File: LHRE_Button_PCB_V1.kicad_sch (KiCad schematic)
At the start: 19 parts, among them J1 Conn_01x12_Female, J2 Conn_01x12_Female, J3 Conn_01x02_Female, SW1 Dashboard_Button, SW2 Dashboard_Button, SW3 Dashboard_Button, SW4 Dashboard_Button, SW5 Dashboard_Button, SW6 Dashboard_Button

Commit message: board proto
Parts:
- added J3: Conn_01x02_Female, Connector_Wire:SolderWire-0.1sqmm_1x02_P3.6mm_D0.4mm_OD1mm, symbol Connector:Conn_01x02_Female
- J1, J2: footprint (none) -> Connector_Molex:Molex_Micro-Fit_3.0_43650-1210_1x12-1MP_P3.00mm_Horizontal
- J4: renamed from J3; footprint (none) -> Connector_Molex:Molex_Micro-Fit_3.0_43650-0210_1x02-1MP_P3.00mm_Horizontal
- R1: footprint Resistor_SMD:R_0201_0603Metric -> Resistor_SMD:R_0603_1608Metric
- R2: renamed from R3; footprint Resistor_SMD:R_0201_0603Metric -> Resistor_SMD:R_0603_1608Metric
- R3: renamed from R4; footprint Resistor_SMD:R_0201_0603Metric -> Resistor_SMD:R_0603_1608Metric
- R4: renamed from R5; footprint Resistor_SMD:R_0201_0603Metric -> Resistor_SMD:R_0603_1608Metric
- R5: renamed from R6; footprint Resistor_SMD:R_0201_0603Metric -> Resistor_SMD:R_0603_1608Metric
- R6: renamed from R7; footprint Resistor_SMD:R_0201_0603Metric -> Resistor_SMD:R_0603_1608Metric
- R7: renamed from R8; footprint Resistor_SMD:R_0201_0603Metric -> Resistor_SMD:R_0603_1608Metric
- R8: renamed from R2; footprint Resistor_SMD:R_0201_0603Metric -> Resistor_SMD:R_0603_1608Metric
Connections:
- net 12V_L: now also J1.11 (Pin_11), J1.5 (Pin_5), SW1.1, SW2.1, SW3.1; no longer J1.10 (Pin_10), J1.12 (Pin_12), SW1. (5), SW2. (5), SW3. (5)
- net 12V_R: now also J2.11 (Pin_11), J2.5 (Pin_5), SW4.1, SW5.1, SW6.1; no longer J2.10 (Pin_10), J2.12 (Pin_12), SW4. (5), SW5. (5), SW6. (5)
- net AMS: now also J1.12 (Pin_12); no longer J1.3 (Pin_3)
- net GND: now also SW4.5, SW5.5, SW6.5; no longer D1.1 (K), J1.1 (Pin_1), R2.1, R3.1, R4.1, SW1. (5), SW2. (5), SW3. (5), SW4. (5), SW5. (5), SW6. (5)
- net IMD: now also J2.12 (Pin_12); no longer J2.3 (Pin_3)
- net MCU_SIG1: now also J1.10 (Pin_10), SW1.4; no longer J1.6 (Pin_6), SW1. (5)
- net MCU_SIG2: now also J1.7 (Pin_7), SW2.4; no longer J1.5 (Pin_5), SW2. (5)
- net MCU_SIG3: now also SW3.4; no longer SW3. (5)
- net MCU_SIG4: now also J2.10 (Pin_10), SW4.4; no longer J2.6 (Pin_6), SW4. (5)
- net MCU_SIG5: now also J2.7 (Pin_7), SW5.4; no longer J2.5 (Pin_5), SW5. (5)
- net MCU_SIG6: now also SW6.4; no longer SW6. (5)
- net SHTDWN_IN: now also J3.1 (Pin_1)
- net SHTDWN_OUT: now also J3.2 (Pin_2)
- net SW1_OUT: now also J1.9 (Pin_9), SW1.2; no longer J1.11 (Pin_11), SW1. (5)
- net SW2_OUT: now also J1.6 (Pin_6), SW2.2; no longer J1.9 (Pin_9), SW2. (5)
- net SW3_OUT: now also J1.3 (Pin_3), SW3.2; no longer J1.7 (Pin_7), SW3. (5)
- net SW4_OUT: now also J2.9 (Pin_9), SW4.2; no longer J2.11 (Pin_11), SW4. (5)
- net SW5_OUT: now also J2.6 (Pin_6), SW5.2; no longer J2.9 (Pin_9), SW5. (5)
- net SW6_OUT: now also J2.3 (Pin_3), SW6.2; no longer J2.7 (Pin_7), SW6. (5)
- new net GND1: D1.1 (K), J1.1 (Pin_1), R2.1, R3.1, R4.1, SW1.5, SW2.5, SW3.5
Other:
- removed sheet SEPIC_CAD_L
- added sheet SEPIC_CAD (SEPIC_L.kicad_sch)
- sheet SEPIC_CAD_R: file ../AccumulatorHUD_2023/2023KicadLibrary-main/Standardized Subsheets/SEPIC_CAD.kicad_sch -> ../../AccumulatorHUD_2023/2023KicadLibrary-main/Standardized Subsheets/SEPIC_CAD.kicad_sch

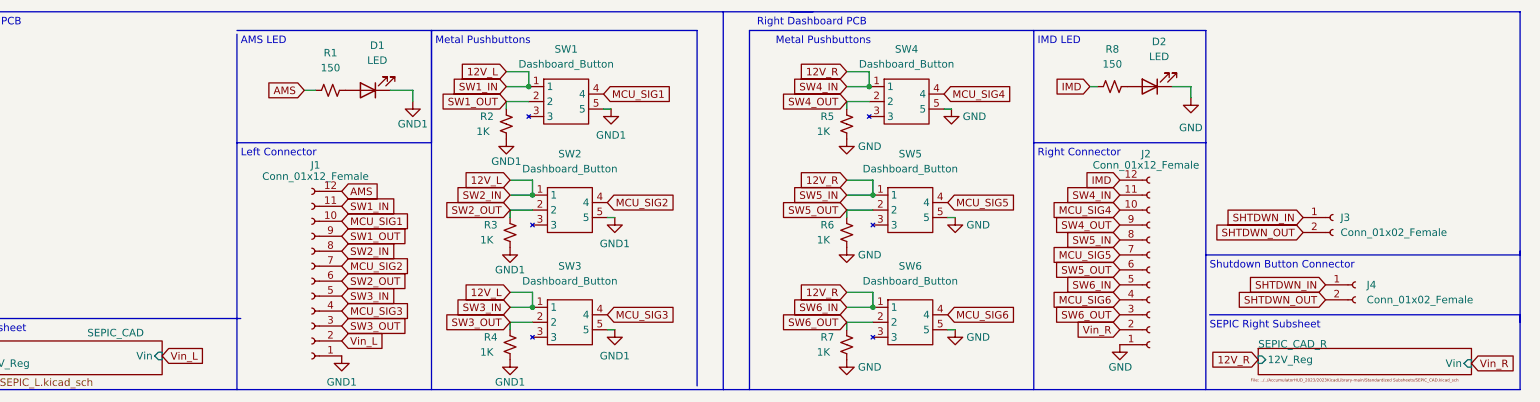
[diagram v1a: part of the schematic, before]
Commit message: updated dash PCB
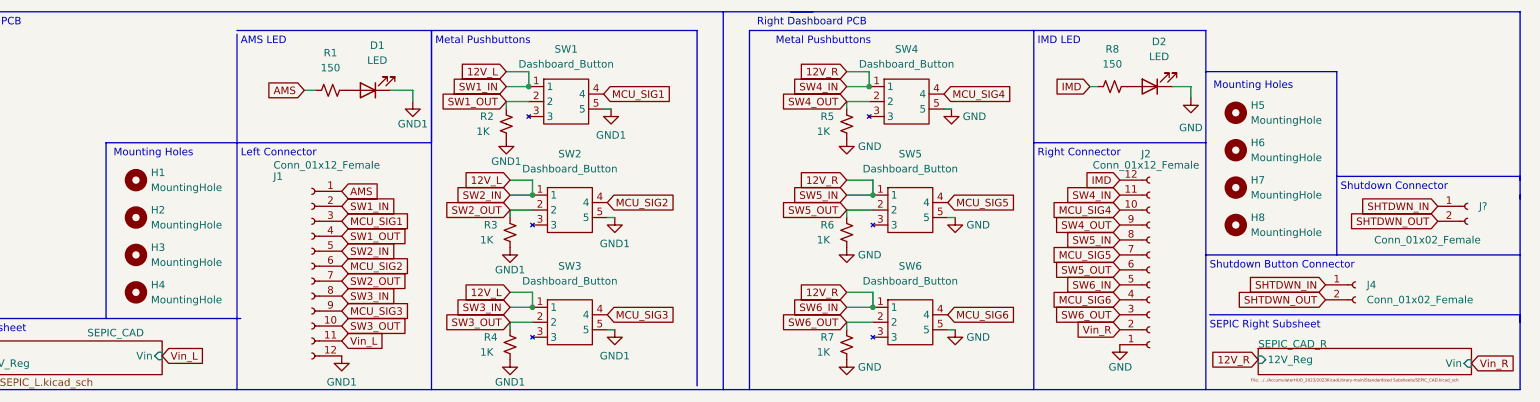
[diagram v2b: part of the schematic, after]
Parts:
- removed J3: Conn_01x02_Female, Connector_Wire:SolderWire-0.1sqmm_1x02_P3.6mm_D0.4mm_OD1mm, symbol Connector:Conn_01x02_Female
- added H1, H2, H3, H4, H5, H6, H7, H8: MountingHole, MountingHole:MountingHole_3.5mm, symbol Mechanical:MountingHole
- added J?: Conn_01x02_Female, Connector_Wire:SolderWire-0.5sqmm_1x02_P4.8mm_D0.9mm_OD2.3mm, symbol Connector:Conn_01x02_Female
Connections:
- net 12V_L: now also J1.2 (Pin_2); no longer J1.11 (Pin_11)
- net AMS: now also J1.1 (Pin_1); no longer J1.12 (Pin_12)
- net GND1: now also J1.12 (Pin_12); no longer J1.1 (Pin_1)
- net MCU_SIG1: now also J1.3 (Pin_3); no longer J1.10 (Pin_10)
- net MCU_SIG2: now also J1.6 (Pin_6); no longer J1.7 (Pin_7)
- net MCU_SIG3: now also J1.9 (Pin_9); no longer J1.4 (Pin_4)
- net SHTDWN_IN: now also J?.1 (Pin_1)
- net SHTDWN_OUT: now also J?.2 (Pin_2)
- net SW1_OUT: now also J1.4 (Pin_4); no longer J1.9 (Pin_9)
- net SW2_OUT: now also J1.7 (Pin_7); no longer J1.6 (Pin_6)
- net SW3_OUT: now also J1.10 (Pin_10); no longer J1.3 (Pin_3)
- net Vin_L: now also J1.11 (Pin_11); no longer J1.2 (Pin_2)
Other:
- note added: "Mounting Holes"
- note added: "Shutdown Connector"
- moved on the sheet: J1

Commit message: REV2
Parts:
- removed D1, D2: LED, Dashboard_LED:LEDC1608X80N, symbol Device:LED
- removed J1, J2: Conn_01x12_Female, Connector_Molex:Molex_Micro-Fit_3.0_43650-1210_1x12-1MP_P3.00mm_Horizontal, symbol Connector:Conn_01x12_Female
- removed J4: Conn_01x02_Female, Connector_Molex:Molex_Micro-Fit_3.0_43650-0210_1x02-1MP_P3.00mm_Horizontal, symbol Connector:Conn_01x02_Female
- removed J?: Conn_01x02_Female, Connector_Wire:SolderWire-0.5sqmm_1x02_P4.8mm_D0.9mm_OD2.3mm, symbol Connector:Conn_01x02_Female
- removed R7: 1K, Resistor_SMD:R_0603_1608Metric, symbol Device:R_Small_US
- removed SW2, SW3, SW4: Dashboard_Button, Dashboard_LED:Dashboard_Btn, symbol Dashboard:Dashboard_Button
- added J1, J2, J3, J7: Conn_01x02, Connector_Molex:Molex_Micro-Fit_3.0_43650-0215_1x02_P3.00mm_Vertical, symbol Connector_Generic:Conn_01x02
- added J4, J5: Conn_01x08, Connector_Molex:Molex_Micro-Fit_3.0_43650-0800_1x08_P3.00mm_Horizontal, symbol Connector_Generic:Conn_01x08
- added J6: Conn_01x12, Connector_Molex:Molex_Micro-Fit_3.0_43045-1212_2x06_P3.00mm_Vertical, symbol Connector_Generic:Conn_01x12
- added R1, R12, R13, R14, R15, R16, R17: 10k, Resistor_SMD:R_0603_1608Metric, symbol Device:R_Small_US
- added R10, R11, R18, R19, R20, R9: 470, Resistor_SMD:R_0603_1608Metric, symbol Device:R_Small_US
- added SW1, SW2, SW3, SW7, SW8, SW9: SW_DIP_x06, Through_DIP_6:18253604, symbol Switch:SW_DIP_x06
- added SW10, SW11, SW12: Dashboard_Button, Dashboard_LED:Dashboard_Btn, symbol Dashboard:Dashboard_Button
- R2, R3, R4, R5, R6: value 1K -> 10k
- renumbered R1 to R7, SW1 to SW4
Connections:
- net 12V_L: now also R3.1, R5.1, R1.1, SW1.5, SW2.5, SW3.5; no longer SW4.1
- net 12V_R: now also R12.1, R14.1, R16.1, SW7.5, SW8.5, SW9.5; no longer SW5.1, SW6.1
- net AMS: now also J4.2 (Pin_2)
- net GND: now also J2.2 (Pin_2), J5.1 (Pin_1), J6.6 (Pin_6), R13.1, R15.1, R17.1, SW7.6, SW8.6, SW9.6; no longer R5.1, R6.1, SW5.5, SW6.5
- net GND1: now also R6.1, J1.2 (Pin_2), J4.8 (Pin_8), SW1.6, SW2.6, SW3.6; no longer R3.1, SW4.5
- net IMD: now also J6.7 (Pin_7)
- net SHTDWN_IN: now also J3.1 (Pin_1), J6.10 (Pin_10)
- net SHTDWN_OUT: now also J4.4 (Pin_4), J7.2 (Pin_2)
- net SW1_OUT: now also J4.1 (Pin_1), SW1.3, SW1.4; no longer R2.2
- net SW2_OUT: now also SW5.2, J4.3 (Pin_3), SW2.3, SW2.4; no longer R3.2
- net SW3_OUT: now also SW6.2, J4.6 (Pin_6), SW3.3, SW3.4; no longer R4.2
- net SW4_OUT: now also J6.4 (Pin_4), SW10.2, SW7.3, SW7.4; no longer R5.2
- net SW5_OUT: now also J6.5 (Pin_5), SW11.2, SW8.3, SW8.4; no longer R6.2, SW5.2
- net SW6_OUT: now also J6.12 (Pin_12), SW12.2, SW9.3, SW9.4; no longer SW6.2
- net Vin_L: now also J4.7 (Pin_7)
- net Vin_R: now also J5.2 (Pin_2), J6.11 (Pin_11)
- net at R8.2: now also J2.1 (Pin_1)
- net at R7.2: now also J1.1 (Pin_1)
- net MCU_SIG1 renamed P11
- net P11: now also SW1.10, SW1.8
- net MCU_SIG5 renamed P21
- net P21: now also SW2.10, SW2.8
- net MCU_SIG6 renamed P31
- net P31: now also SW3.10, SW3.8
- new net: R11.2, SW6.5
- new net: R19.2, SW11.5
- new net: R5.2, SW3.2
- new net: R15.2, SW8.1
- new net: R18.2, SW10.5
- new net: R10.2, SW5.5
- new net: R17.2, SW9.1
- new net: R4.2, SW2.1
- new net: R3.2, SW2.2
- new net: R16.2, SW9.2
- new net: R9.2, SW4.5
- new net: R6.2, SW3.1
- new net: R20.2, SW12.5
- new net: R14.2, SW8.2
- new net: R13.2, SW7.1
- new net: R1.2, SW1.2
- new net: R12.2, SW7.2
- new net: R2.2, SW1.1
- new net AMS_R: J5.7 (Pin_7), J6.8 (Pin_8)
- new net G11: R9.1, SW1.7, SW1.9
- new net G21: R10.1, SW2.7, SW2.9
- new net G31: R11.1, SW3.7, SW3.9
- new net G41: R18.1, SW7.7, SW7.9
- new net G51: R19.1, SW8.7, SW8.9
- new net G61: R20.1, SW9.7, SW9.9
- new net INRTA_IN: J4.5 (Pin_5), J7.1 (Pin_1)
- new net INRTA_IN_R: J3.2 (Pin_2), J5.4 (Pin_4)
- new net P41: SW10.4, SW7.10, SW7.8
- new net P51: SW11.4, SW8.10, SW8.8
- new net P61: SW12.4, SW9.10, SW9.8
- new net SHTDWN_OUT_R: J5.5 (Pin_5), J6.9 (Pin_9)
- new net SW1_IN: SW1.11, SW1.12, SW4.1
- new net SW1_OUT_R: J5.8 (Pin_8), J6.1 (Pin_1)
- new net SW2_IN: SW2.11, SW2.12, SW5.1
- new net SW2_OUT_R: J5.6 (Pin_6), J6.2 (Pin_2)
- new net SW3_IN: SW3.11, SW3.12, SW6.1
- new net SW3_OUT_R: J5.3 (Pin_3), J6.3 (Pin_3)
- new net SW4_IN: SW10.1, SW7.11, SW7.12
- new net SW5_IN: SW11.1, SW8.11, SW8.12
- new net SW6_IN: SW12.1, SW9.11, SW9.12
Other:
- removed sheet SEPIC_CAD_R
- note added: "Exit Connector Left"
- note added: "Exit Connector Right"
- note added: "In Connector Right"
- note added: "Inertia Switch"
- note added: "Latching Buttons"
- note added: "Momentary Buttons"
- note added: "Mounting Holes Left"
- note added: "Mounting Holes Right"
- note removed: "Left Connector"
- note removed: "Left Dashboard PCB"
- note removed: "Metal Pushbuttons"
- note removed: "Mounting Holes"
- note removed: "Right Connector"
- note removed: "Right Dashboard PCB"
- note removed: "SEPIC Right Subsheet"
- note removed: "Shutdown Button Connector"
- moved on the sheet: H1, H2, H3, H4, H5, H6, H7, H8, R7, R8, SW4

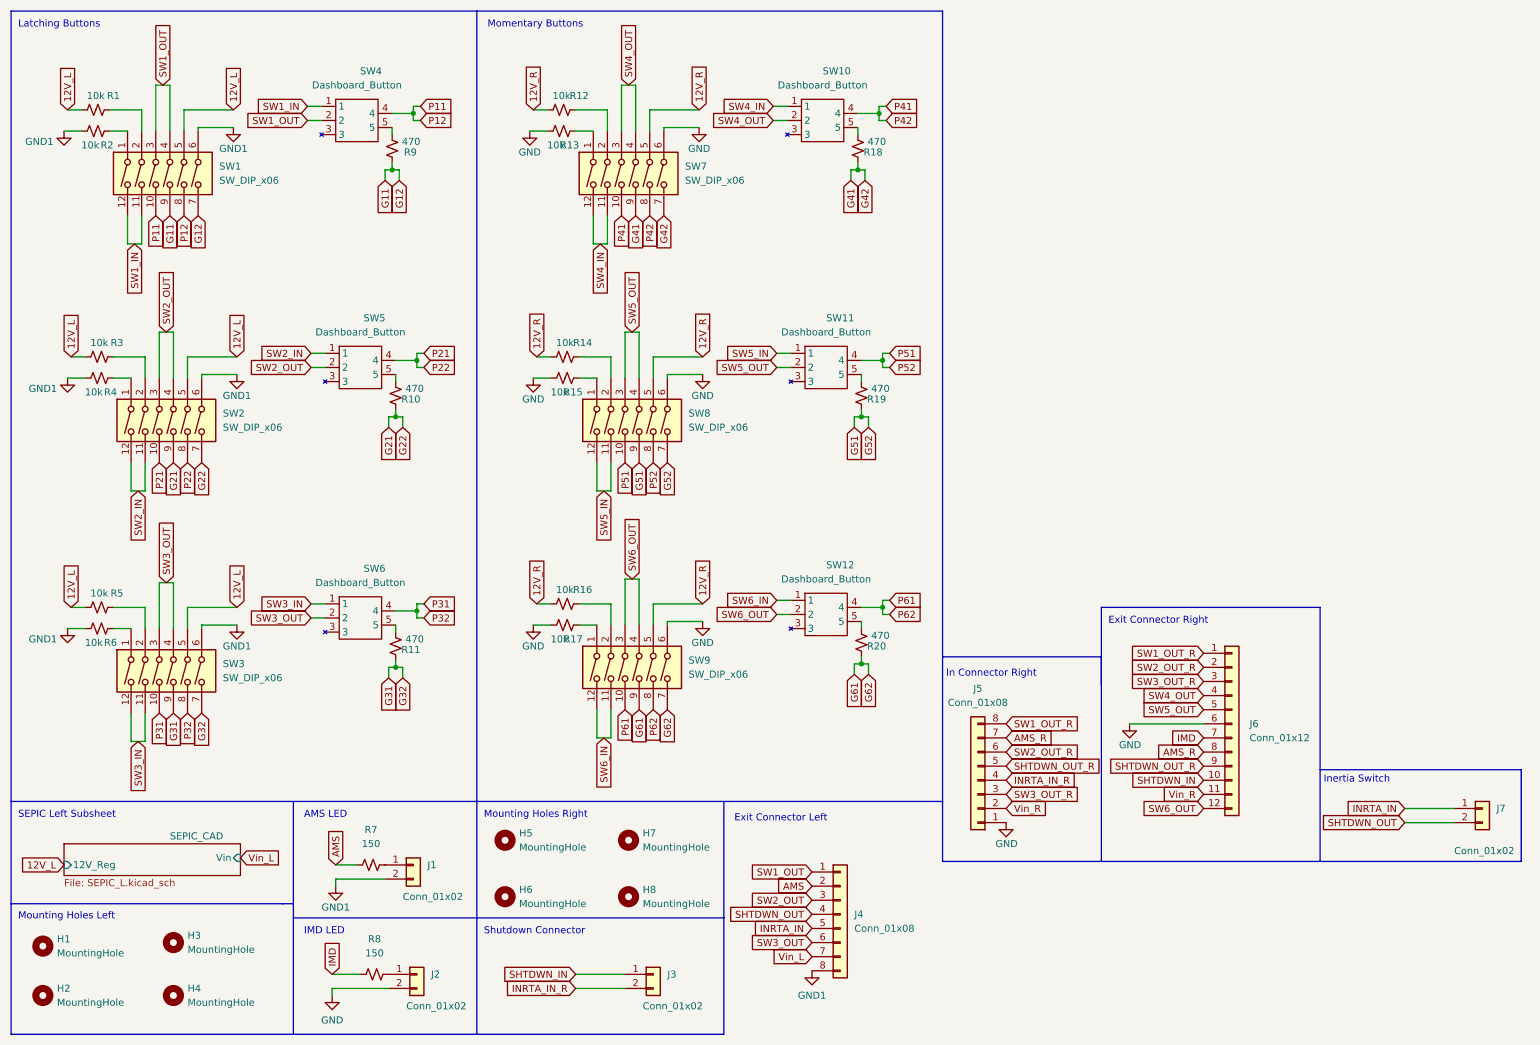
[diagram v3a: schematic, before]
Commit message: flipped connectors
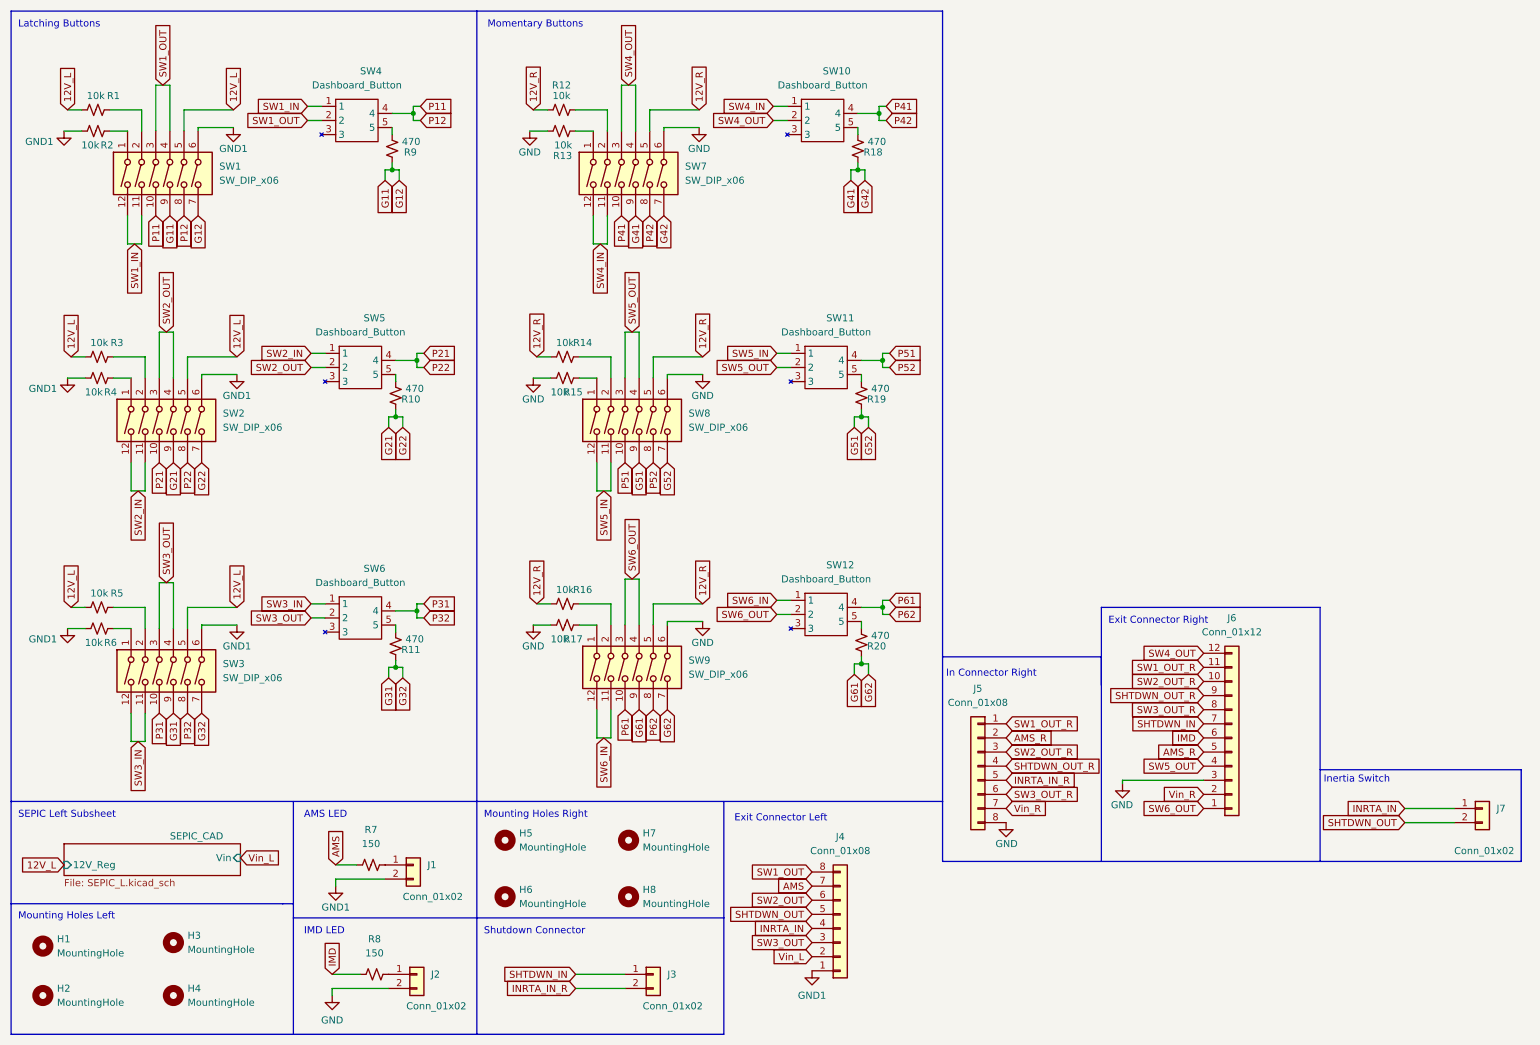
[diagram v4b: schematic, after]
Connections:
- net AMS: now also J4.7 (Pin_7); no longer J4.2 (Pin_2)
- net AMS_R: now also J5.2 (Pin_2), J6.5 (Pin_5); no longer J5.7 (Pin_7), J6.8 (Pin_8)
- net GND: now also J5.8 (Pin_8), J6.3 (Pin_3); no longer J5.1 (Pin_1), J6.6 (Pin_6)
- net GND1: now also J4.1 (Pin_1); no longer J4.8 (Pin_8)
- net IMD: now also J6.6 (Pin_6); no longer J6.7 (Pin_7)
- net INRTA_IN: now also J4.4 (Pin_4); no longer J4.5 (Pin_5)
- net INRTA_IN_R: now also J5.5 (Pin_5); no longer J5.4 (Pin_4)
- net SHTDWN_IN: now also J6.7 (Pin_7); no longer J6.10 (Pin_10)
- net SHTDWN_OUT: now also J4.5 (Pin_5); no longer J4.4 (Pin_4)
- net SHTDWN_OUT_R: now also J5.4 (Pin_4); no longer J5.5 (Pin_5)
- net SW1_OUT: now also J4.8 (Pin_8); no longer J4.1 (Pin_1)
- net SW1_OUT_R: now also J5.1 (Pin_1), J6.11 (Pin_11); no longer J5.8 (Pin_8), J6.1 (Pin_1)
- net SW2_OUT: now also J4.6 (Pin_6); no longer J4.3 (Pin_3)
- net SW2_OUT_R: now also J5.3 (Pin_3), J6.10 (Pin_10); no longer J5.6 (Pin_6), J6.2 (Pin_2)
- net SW3_OUT: now also J4.3 (Pin_3); no longer J4.6 (Pin_6)
- net SW3_OUT_R: now also J5.6 (Pin_6), J6.8 (Pin_8); no longer J5.3 (Pin_3), J6.3 (Pin_3)
- net SW4_OUT: now also J6.12 (Pin_12); no longer J6.4 (Pin_4)
- net SW5_OUT: now also J6.4 (Pin_4); no longer J6.5 (Pin_5)
- net SW6_OUT: now also J6.1 (Pin_1); no longer J6.12 (Pin_12)
- net Vin_L: now also J4.2 (Pin_2); no longer J4.7 (Pin_7)
- net Vin_R: now also J5.7 (Pin_7), J6.2 (Pin_2); no longer J5.2 (Pin_2), J6.11 (Pin_11)
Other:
- moved on the sheet: J5
